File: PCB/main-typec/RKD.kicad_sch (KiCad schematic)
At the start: 87 parts, among them J10 Conn_01x04_Male, J11 Conn_02x06_Odd_Even, J12 Conn_01x06, J13 Conn_01x03, J14 Conn_01x04, J15 Conn_01x04, J2 Conn_02x02_Odd_Even, J3 Conn_02x04_Odd_Even, J4 Conn_02x02_Odd_Even, J5 Conn_02x04_Odd_Even, J6 Conn_02x04_Odd_Even, J7 Conn_02x02_Odd_Even, J8 Conn_02x02_Odd_Even, J9 Conn_02x04_Odd_Even, K1 Key, K2 Key, K3 Key, K4 Key, K5 Key, K6 Key, P1 USB_C_Plug_USB2.0, SW2 SW_DIP_x04, SW3 SW_Push, SW5 SW_Push, SW6 RotaryEncoder_Switch, SW7 SW_Push, SW8 RotaryEncoder_Switch, U1 W25Q32JV, U2 RP2040, U3 CH9329, U4 AP1117-33, Y1 Crystal 12MHZ HC49, Y2 Crystal_GND24 12MHZ 3225

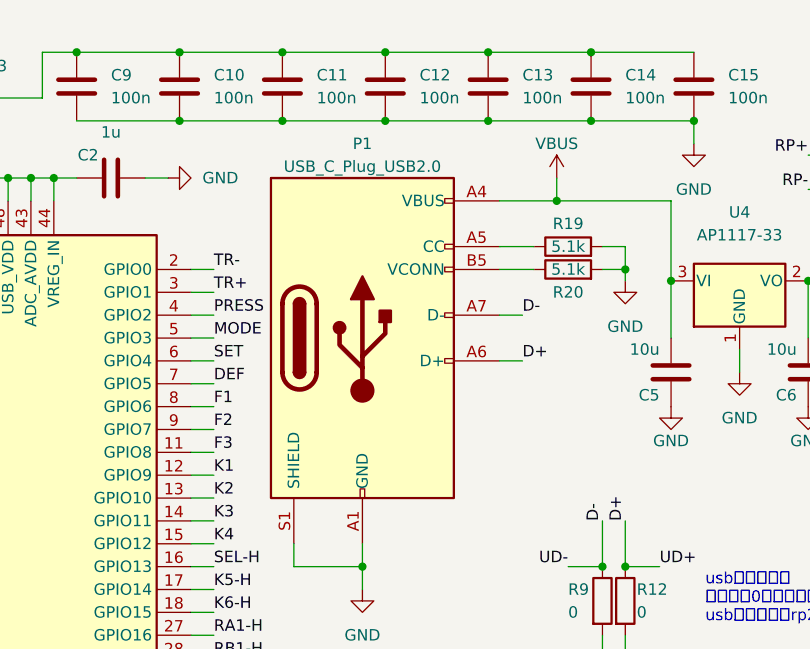
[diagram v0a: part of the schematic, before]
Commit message: 修复typec版本的接口只能在特定一面使用
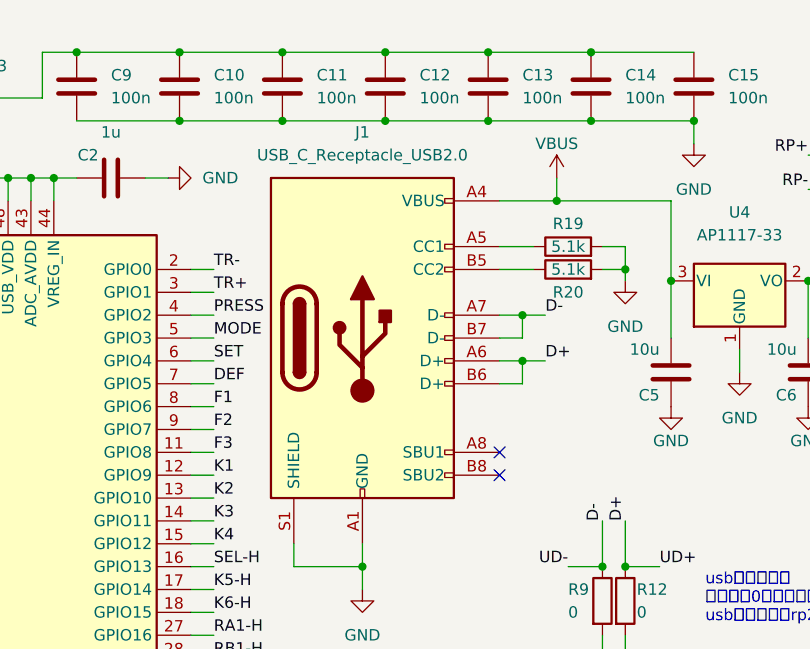
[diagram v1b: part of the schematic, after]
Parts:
- removed P1: USB_C_Plug_USB2.0, Connector_USB:USB_C_Receptacle_HRO_TYPE-C-31-M-12, symbol Connector:USB_C_Plug_USB2.0
- added J1: USB_C_Receptacle_USB2.0, Connector_USB:USB_C_Receptacle_HRO_TYPE-C-31-M-12, symbol Connector:USB_C_Receptacle_USB2.0
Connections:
- net D+: now also J1.A6 (D+), J1.B6 (D+)
- net D-: now also J1.A7 (D-), J1.B7 (D-)
- net GND: now also J1.A1 (GND), J1.A12 (GND), J1.B1 (GND), J1.B12 (GND), J1.S1 (SHIELD)
- net VBUS: now also J1.A4 (VBUS), J1.A9 (VBUS), J1.B4 (VBUS), J1.B9 (VBUS)
- net at R20.1: now also J1.B5 (CC2)
- net at R19.1: now also J1.A5 (CC1)
- no-connect marks 16 -> 18
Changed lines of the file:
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@@
   (title_block
     (title "RKD-main-typec")
-    (date "2023-01-30")
-    (rev "35")
+    (date "2023-02-04")
+    (rev "37")
     (company "PCX-LK")
     (comment 1 "https://github.com/PCX-LK/RKD")
@@
   (junction (at 175.26 41.91) (diameter 0) (color 0 0 0 0)
   )
+  (junction (at 158.75 45.72) (diameter 0) (color 0 0 0 0)
+  )
   (junction (at 69.85 151.13) (diameter 0) (color 0 0 0 0)
   )
@@
   (junction (at 87.63 186.69) (diameter 0) (color 0 0 0 0)
   )
+  (junction (at 158.75 50.8) (diameter 0) (color 0 0 0 0)
+  )
   (junction (at 72.39 24.13) (diameter 0) (color 0 0 0 0)
   )
@@
   (no_connect (at 132.08 182.88))
   (no_connect (at 251.46 49.53))
+  (no_connect (at 156.21 63.5))
   (no_connect (at 256.54 110.49))
+  (no_connect (at 156.21 60.96))
   (wire (pts (xy 172.72 144.78) (xy 171.45 144.78))
     (stroke (width 0) (type default) (color 0 0 0 0))
@@
     (stroke (width 0) (type default) (color 0 0 0 0))
   )
+  (wire (pts (xy 158.75 48.26) (xy 156.21 48.26))
+    (stroke (width 0) (type default) (color 0 0 0 0))
+  )
   (wire (pts (xy 39.37 187.96) (xy 39.37 185.42))
     (stroke (width 0) (type default) (color 0 0 0 0))
@@
     (stroke (width 0) (type default) (color 0 0 0 0))
   )
+  (wire (pts (xy 158.75 45.72) (xy 161.29 45.72))
+    (stroke (width 0) (type default) (color 0 0 0 0))
+  )
   (wire (pts (xy 36.83 35.56) (xy 36.83 36.83))
     (stroke (width 0) (type default) (color 0 0 0 0))
@@
     (stroke (width 0) (type default) (color 0 0 0 0))
   )
+  (wire (pts (xy 158.75 50.8) (xy 161.29 50.8))
+    (stroke (width 0) (type default) (color 0 0 0 0))
+  )
   (wire (pts (xy 177.8 142.24) (xy 177.8 144.78))
     (stroke (width 0) (type default) (color 0 0 0 0))
   )
+  (wire (pts (xy 158.75 45.72) (xy 158.75 48.26))
+    (stroke (width 0) (type default) (color 0 0 0 0))
+  )
   (wire (pts (xy 218.44 36.83) (xy 217.17 36.83))
     (stroke (width 0) (type default) (color 0 0 0 0))
@@
     (stroke (width 0) (type default) (color 0 0 0 0))
   )
+  (wire (pts (xy 158.75 53.34) (xy 156.21 53.34))
+    (stroke (width 0) (type default) (color 0 0 0 0))
+  )
   (wire (pts (xy 232.41 63.5) (xy 232.41 66.04))
     (stroke (width 0) (type default) (color 0 0 0 0))
@@
     (stroke (width 0) (type default) (color 0 0 0 0))
   )
+  (wire (pts (xy 158.75 50.8) (xy 158.75 53.34))
+    (stroke (width 0) (type default) (color 0 0 0 0))
+  )
   (image (at 276.86 173.99) (scale 0.145832)
     (data
@@
     (effects (font (size 1.27 1.27)) (justify left bottom))
   )
-  (label "D+" (at 158.75 50.8 0)
+  (label "D+" (at 161.29 50.8 0)
     (effects (font (size 1.27 1.27)) (justify left bottom))
   )
@@
     (effects (font (size 1.27 1.27)) (justify left bottom))
   )
-  (label "D-" (at 158.75 45.72 0)
+  (label "D-" (at 161.29 45.72 0)
     (effects (font (size 1.27 1.27)) (justify left bottom))
   )
@@
     (pin "2")
   )
+  (symbol (lib_id "Connector:USB_C_Receptacle_USB2.0") (at 140.97 48.26 0) (unit 1)
+    (in_bom yes) (on_board yes) (fields_autoplaced)
+    (property "Reference" "J1" (id 0) (at 140.97 25.4 0))
+    (property "Value" "USB_C_Receptacle_USB2.0" (id 1) (at 140.97 27.94 0))
+    (property "Footprint" "Connector_USB:USB_C_Receptacle_HRO_TYPE-C-31-M-12" (id 2) (at 144.78 48.26 0)
+      (effects (font (size 1.27 1.27)) hide)
+    )
+    (property "Datasheet" "https://www.usb.org/sites/default/files/documents/usb_type-c.zip" (id 3) (at 144.78 48.26 0)
+      (effects (font (size 1.27 1.27)) hide)
+    )
+    (pin "A1")
+    (pin "A12")
+    (pin "A4")
+    (pin "A5")
+    (pin "A6")
+    (pin "A7")
+    (pin "A8")
+    (pin "A9")
+    (pin "B1")
+    (pin "B12")
+    (pin "B4")
+    (pin "B5")
+    (pin "B6")
+    (pin "B7")
+    (pin "B8")
+    (pin "B9")
+    (pin "S1")
+  )
   (symbol (lib_id "Device:C") (at 255.27 86.36 270) (unit 1)
     (in_bom yes) (on_board yes) (fields_autoplaced)
@@
     (pin "2")
   )
-  (symbol (lib_id "Connector:USB_C_Plug_USB2.0") (at 140.97 48.26 0) (unit 1)
-    (in_bom yes) (on_board yes) (fields_autoplaced)
-    (property "Reference" "P1" (id 0) (at 140.97 26.67 0))
-    (property "Value" "USB_C_Plug_USB2.0" (id 1) (at 140.97 29.21 0))
-    (property "Footprint" "Connector_USB:USB_C_Receptacle_HRO_TYPE-C-31-M-12" (id 2) (at 144.78 48.26 0)
-      (effects (font (size 1.27 1.27)) hide)
-    )
-    (property "Datasheet" "https://www.usb.org/sites/default/files/documents/usb_type-c.zip" (id 3) (at 144.78 48.26 0)
-      (effects (font (size 1.27 1.27)) hide)
-    )
-    (pin "A1")
-    (pin "A12")
-    (pin "A4")
-    (pin "A5")
-    (pin "A6")
-    (pin "A7")
-    (pin "A9")
-    (pin "B1")
-    (pin "B12")
-    (pin "B4")
-    (pin "B5")
-    (pin "B9")
-    (pin "S1")
-  )
   (symbol (lib_id "power:+3V3") (at 168.91 140.97 0) (unit 1)
     (in_bom yes) (on_board yes)
@@
       (reference "H11") (unit 1) (value "MountingHole") (footprint "foot:HO")
     )
+    (path "/37c14130-5b6b-4bb3-a179-bafe220f11f5"
+      (reference "J1") (unit 1) (value "USB_C_Receptacle_USB2.0") (footprint "Connector_USB:USB_C_Receptacle_HRO_TYPE-C-31-M-12")
+    )
     (path "/9e5886ef-ecb1-4463-801d-76aa53bf1eb1"
       (reference "J2") (unit 1) (value "Conn_02x02_Odd_Even") (footprint "Connector_PinHeader_2.54mm:PinHeader_2x02_P2.54mm_Horizontal")
@@
       (reference "K6") (unit 1) (value "Key") (footprint "foot:Key")
     )
-    (path "/ee30bd49-49ad-49ce-b9f3-23223007ae81"
-      (reference "P1") (unit 1) (value "USB_C_Plug_USB2.0") (footprint "Connector_USB:USB_C_Receptacle_HRO_TYPE-C-31-M-12")
-    )
     (path "/9c696d2e-0037-45e1-924c-75680588093c"

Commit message: fix pcb
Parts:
- U4: value AP1117-33 -> AMS1117-33
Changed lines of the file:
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@@
     (in_bom yes) (on_board yes) (fields_autoplaced)
     (property "Reference" "U4" (id 0) (at 182.88 34.29 0))
-    (property "Value" "AP1117-33" (id 1) (at 182.88 36.83 0))
+    (property "Value" "AMS1117-33" (id 1) (at 182.88 36.83 0))
     (property "Footprint" "Package_TO_SOT_SMD:SOT-223-3_TabPin2" (id 2) (at 182.88 36.83 0)
       (effects (font (size 1.27 1.27)) hide)
@@
     )
     (path "/cb0d88bb-9c4c-4c4d-ad2e-692d2f8e5d90"
-      (reference "U4") (unit 1) (value "AP1117-33") (footprint "Package_TO_SOT_SMD:SOT-223-3_TabPin2")
+      (reference "U4") (unit 1) (value "AMS1117-33") (footprint "Package_TO_SOT_SMD:SOT-223-3_TabPin2")
     )
     (path "/ff4b2401-c0e1-4c1f-9136-1d9dd7534361"
